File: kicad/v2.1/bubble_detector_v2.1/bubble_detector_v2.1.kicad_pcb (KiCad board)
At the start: 2 copper layers, 68.6 x 53.3 mm, 7 parts, among them J1 Power, J2 Digital/PWM, J3 Analog, J4 Digital/PWM, U1 HC-SR04

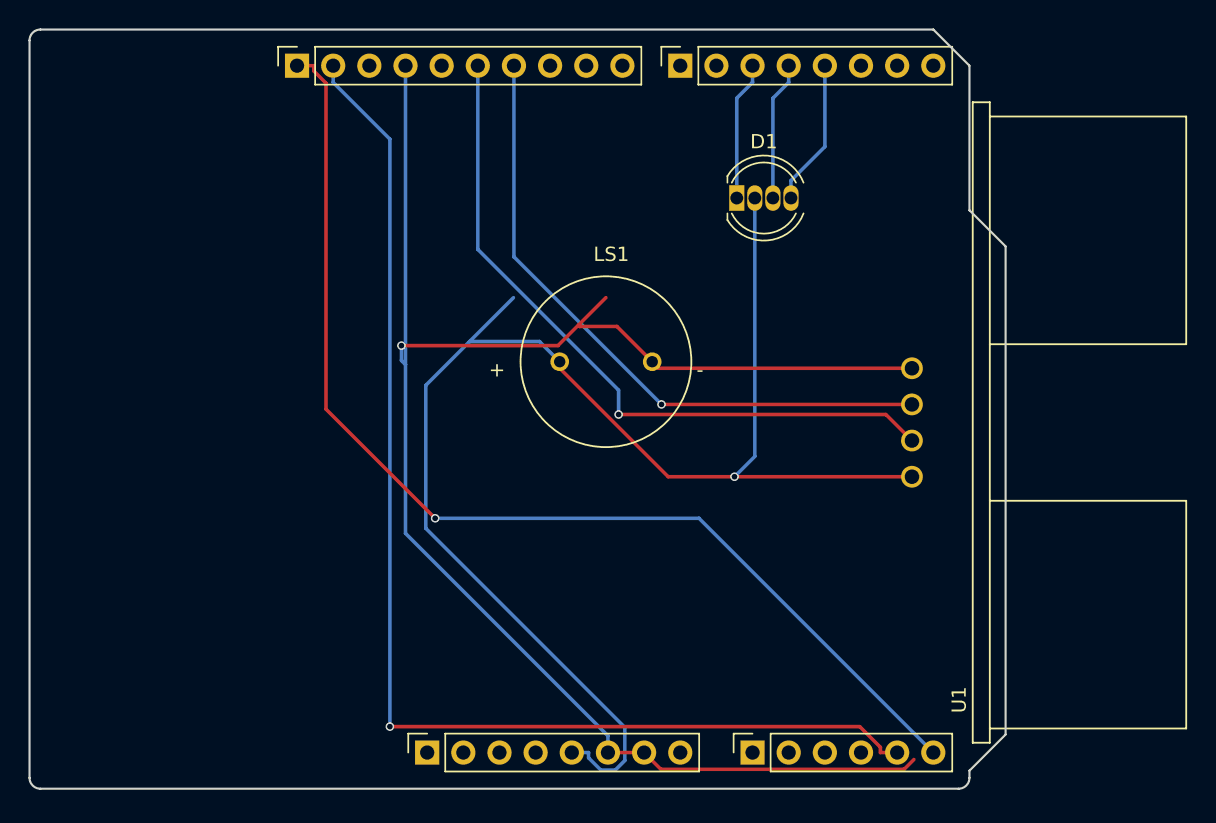
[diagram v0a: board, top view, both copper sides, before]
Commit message: adding arduino library
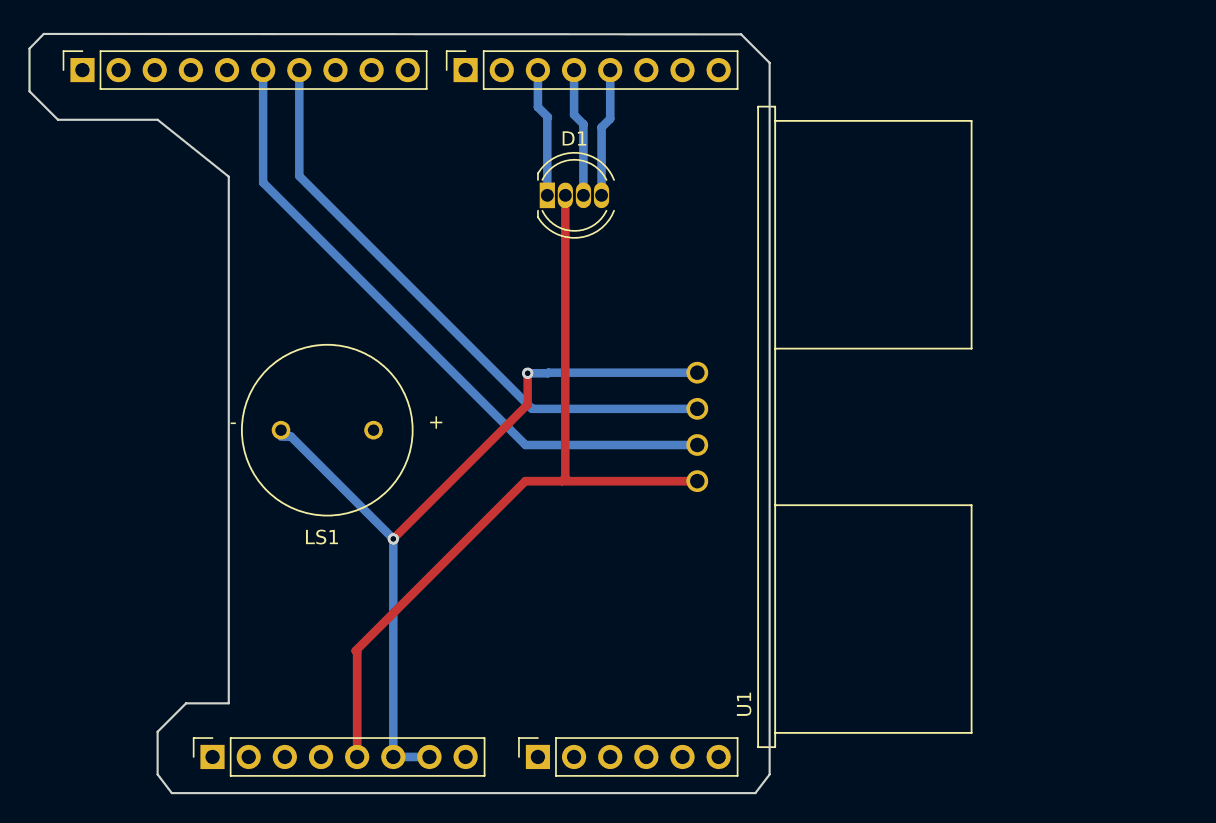
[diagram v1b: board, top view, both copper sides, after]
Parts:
- moved LS1 20.2 mm to (120.9, 74.8), turned to 180 degrees
- moved J2 15.1 mm to (103.7, 49.5)
- moved J3 15.1 mm to (135.7, 97.8)
- moved J4 15.1 mm to (130.6, 49.5)
- moved U1 15.1 mm to (146.9, 74.6)
- moved J1 15.1 mm to (112.9, 97.8)
- moved D1 13.3 mm to (136.4, 58.3)
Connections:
- J1 pad 6: GND -> GND1
- J1 pad 7: GND -> GND1
- J2 pad 1: /SCL/A5 -> /SCL/A5_2
- J2 pad 2: /SDA/A4 -> /SDA/A4_2
- J2 pad 4: GND -> GND2
- J3 pad 5: /SDA/A4 -> /SDA/A4_1
- J3 pad 6: /SCL/A5 -> /SCL/A5_1
- LS1 pad N: GND -> GND1
- LS1 pad P: +5V -> /*9
- U1 pad 4: GND -> GND1
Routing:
- net GND: track 118.3 -> 0.00 mm, vias 1 -> 0
- net /SDA/A4: track 84.7 -> 0.00 mm, vias 1 -> 0
- net /SCL/A5: track 78.3 -> 0.00 mm, vias 1 -> 0
- net GND1: track 0.00 -> 56.2 mm, vias 0 -> 2
- net +5V: track 101.0 -> 56.6 mm, vias 1 -> 0
- net /12: track 50.0 -> 46.0 mm, vias 1 -> 0
- net /*11: track 45.7 -> 42.2 mm, vias 1 -> 0
- net /*3: track 10.3 -> 9.05 mm
- net /4: track 9.76 -> 9.07 mm
- net /*5: track 9.76 -> 9.11 mm
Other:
- board size 68.6 x 53.3 mm -> 52 x 53.3 mm

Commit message: added servo and am working on schematic
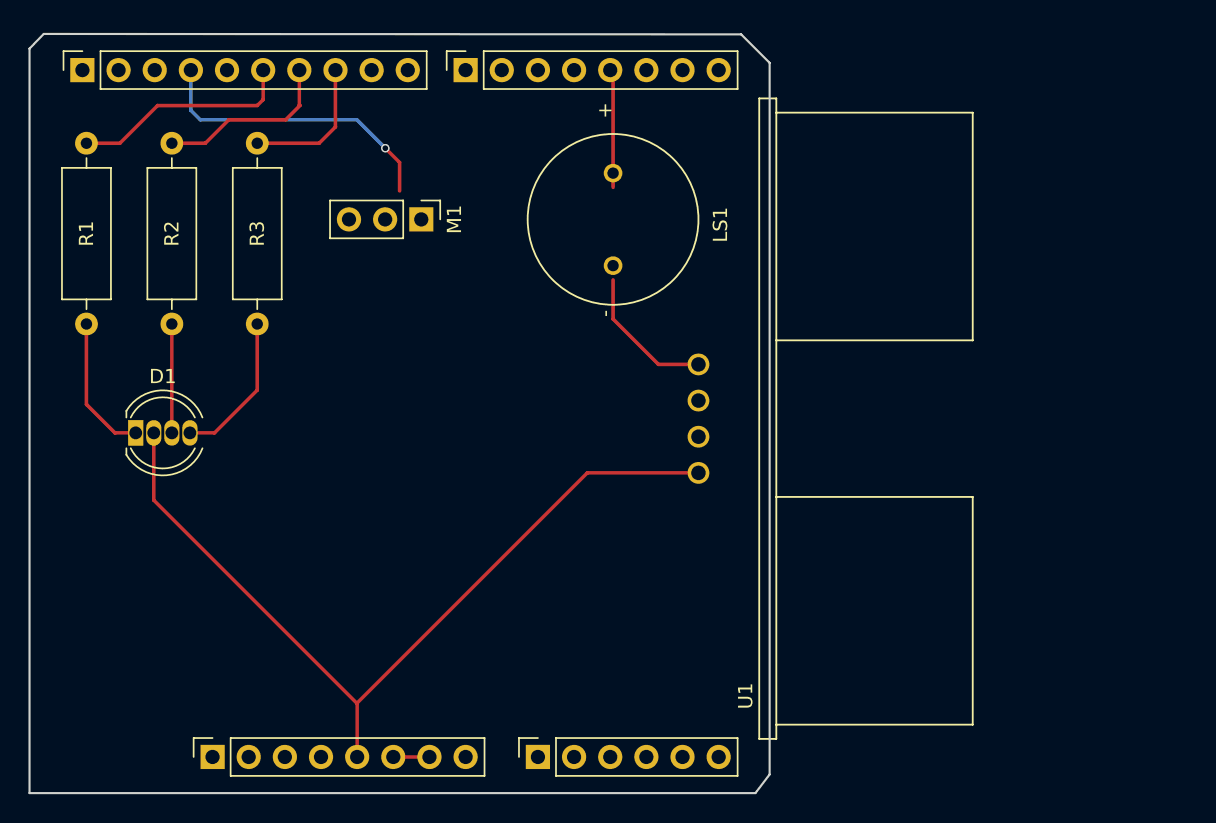
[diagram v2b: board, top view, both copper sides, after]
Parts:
- added M1: Motor_Servo_Hitec, Connector_PinHeader_2.54mm:PinHeader_1x03_P2.54mm_Vertical, F.Cu at (127.5, 60.0)
- added R1: R, Resistor_THT:R_Axial_DIN0309_L9.0mm_D3.2mm_P12.70mm_Horizontal, F.Cu at (104.0, 54.6)
- added R2: R, Resistor_THT:R_Axial_DIN0309_L9.0mm_D3.2mm_P12.70mm_Horizontal, F.Cu at (110.0, 54.6)
- added R3: R, Resistor_THT:R_Axial_DIN0309_L9.0mm_D3.2mm_P12.70mm_Horizontal, F.Cu at (116.0, 54.6)
- moved D1 33.4 mm to (107.5, 75.0)
- moved LS1 25.0 mm to (141.0, 60.0), turned to -90 degrees
- moved U1 0.59 mm to (147.0, 74.0)
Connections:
- net VCC renamed /Vin
- D1 pad 1: /*5 -> Net-(D1-RK)
- D1 pad 3: /4 -> Net-(D1-GK)
- D1 pad 4: /*3 -> Net-(D1-BK)
- LS1 pad P: /*9 -> /*3
- U1 pad 2: /12 -> /*5
- U1 pad 3: /*11 -> /*6
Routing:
- net GND1: track 56.2 -> 12.6 mm, vias 2 -> 0
- net /12: track 46.0 -> 15.8 mm
- net /*11: track 42.2 -> 12.6 mm
- net GND2: track 0.00 -> 21.0 mm, vias 0 -> 1
- net Net-(D1-BK): track 0.00 -> 10.6 mm
- net /*10: track 0.00 -> 9.96 mm
- net Net-(D1-RK): track 0.00 -> 9.94 mm
- net /*5: track 9.11 -> 0.00 mm
- net /4: track 9.07 -> 0.00 mm
- net Net-(D1-GK): track 0.00 -> 7.65 mm
- net +5V: track 56.6 -> 59.4 mm
- net /*3: track 9.05 -> 8.32 mm
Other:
- outline, holes or cut-outs redrawn

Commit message: Added all componenets, generated gerbers
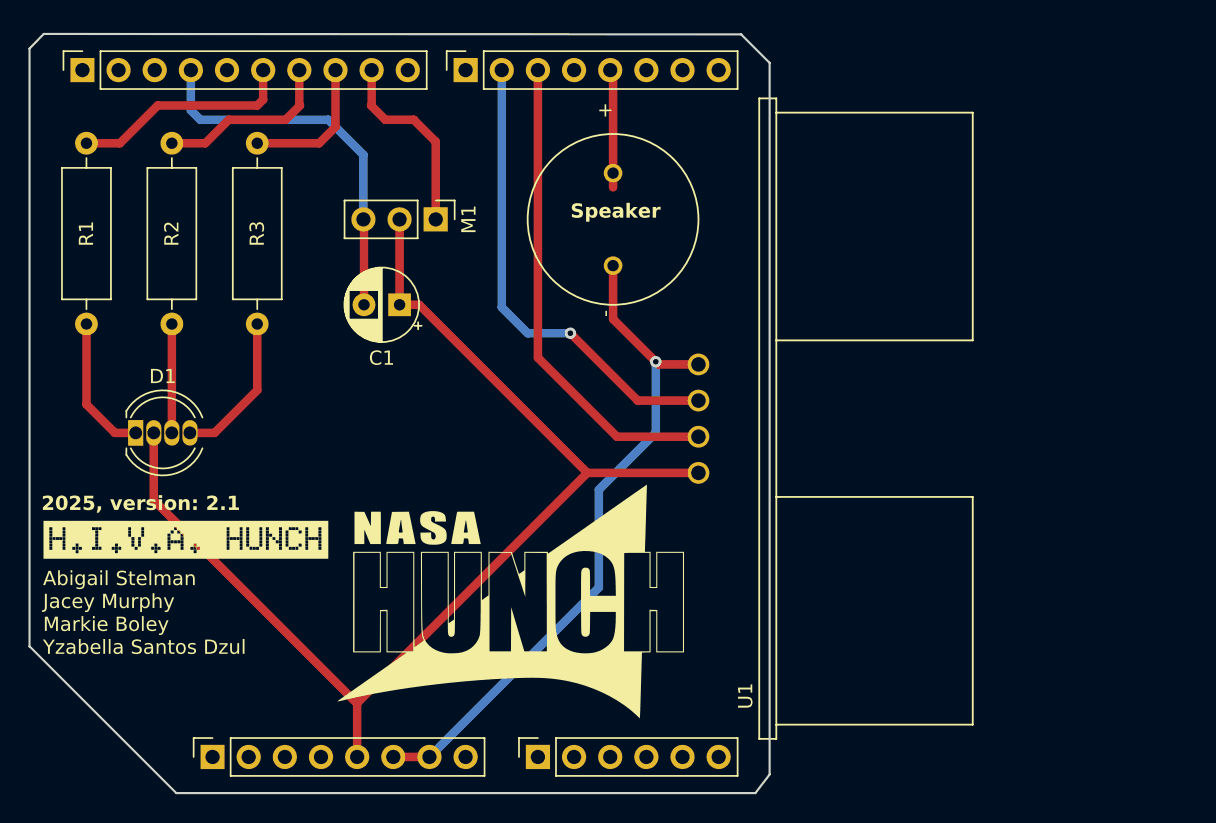
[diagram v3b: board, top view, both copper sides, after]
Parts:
- added C1: C_Polarized, Capacitor_THT:CP_Radial_D5.0mm_P2.50mm, F.Cu at (126.0, 66.0)
- added G***: LOGO, silk_hiva_hunch_name:silk_hiva_hunch_name, F.Cu at (111.0, 82.5)
- added G***: LOGO, silk_hiva_hunch:silk_hiva_hunch_back, F.Cu at (134.0, 87.0)
- moved M1 1.01 mm to (128.5, 60.0)
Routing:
- net GND1: track 12.6 -> 48.0 mm, vias 0 -> 1
- net /*5: track 0.00 -> 33.8 mm
- net /*6: track 0.00 -> 33.2 mm, vias 0 -> 1
- net +5V: track 59.4 -> 83.5 mm
- net /*9: track 0.00 -> 13.6 mm
- net GND2: track 21.0 -> 26.8 mm, vias 1 -> 0
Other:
- outline, holes or cut-outs redrawn
- board text added: "2025, version: 2.1"
- board text added: "Abigail Stelman Jacey Murphy Markie Boley Yzabella Santos Dzul"
- board text added: "Speaker"

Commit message: finished design review w team, adding last touches
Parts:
- moved G*** 1.96 mm to (109.9, 84.2)
- moved G*** 1.00 mm to (134.0, 86.0)
- moved U1 1.00 mm to (146.0, 74.0)
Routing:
- net GND1: track 48.0 -> 47.0 mm
- net /*6: track 33.2 -> 32.2 mm
- net /*5: track 33.8 -> 32.8 mm
- net +5V: track 83.5 -> 82.5 mm
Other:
- outline, holes or cut-outs redrawn
- board text added: "2025, Version: 2.1"
- board text removed: "2025, version: 2.1"

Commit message: continuted adding last touches
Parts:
- moved U1 1.00 mm to (147.0, 74.0)
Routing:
- net GND2: track 26.8 -> 25.6 mm
- net GND1: track 47.0 -> 48.1 mm
- net /*5: track 32.8 -> 33.8 mm
- net /*3: track 8.32 -> 7.32 mm
- net +5V: track 82.5 -> 83.5 mm
- net /*6: track 32.2 -> 31.6 mm
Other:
- board text added: "+5V"
- board text added: "-"
- board text added: "12"
- board text added: "5V"
- board text added: "Echo"
- board text added: "GND"
- board text added: "Trig"
- board text added: "~10"
- board text added: "~11"
- board text added: "~3"
- board text added: "~5"
- board text added: "~6"
- board text added: "~9"

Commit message: added osh park order pdf
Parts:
- added G***: LOGO, nasa:meatball, B.Cu at (127.0, 75.0)
- moved G*** 0.29 mm to (109.6, 84.1)
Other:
- board size 52 x 53.3 mm -> 54 x 53 mm
- board text added: "100 ohm"
- board text added: "150 ohm"
- board text added: "BLUE"
- board text added: "BROWN"
- board text added: "GREEN"
- board text added: "RED"
- board text added: "YELLOW"
- board text removed: "-"
- board text removed: "5V"
- board text removed: "ICSP"
